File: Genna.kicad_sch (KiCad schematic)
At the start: 12 parts, among them J1 USB_A, J2 Conn_01x09, J3 Conn_01x09, U1 ATmega32U4-M

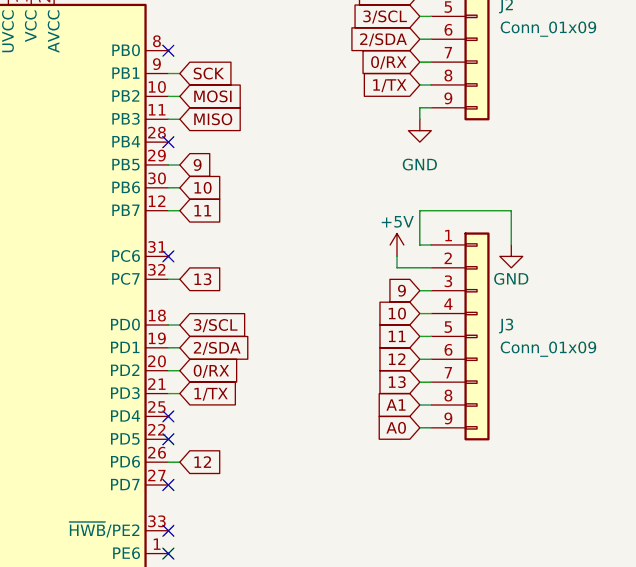
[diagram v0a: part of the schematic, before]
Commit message: changed via dimensions and had to remove an IO
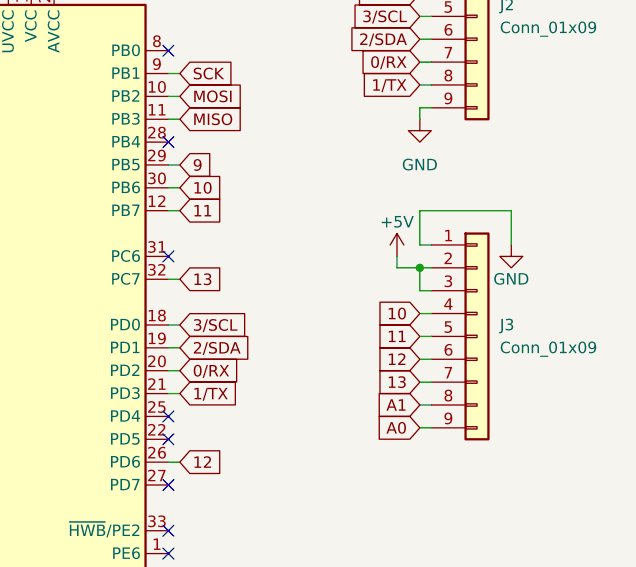
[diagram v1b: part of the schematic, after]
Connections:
- net +5V: now also J3.3 (Pin_3)
- net 9: no longer J3.3 (Pin_3)
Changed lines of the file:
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@@
   (junction (at 168.91 134.62) (diameter 0) (color 0 0 0 0)
+  )
+  (junction (at 214.63 72.39) (diameter 0) (color 0 0 0 0)
   )
   (junction (at 138.43 134.62) (diameter 0) (color 0 0 0 0)
@@
     (stroke (width 0) (type default) (color 0 0 0 0))
   )
+  (wire (pts (xy 214.63 72.39) (xy 215.9 72.39))
+    (stroke (width 0) (type default) (color 0 0 0 0))
+  )
   (wire (pts (xy 154.94 33.02) (xy 171.45 33.02))
     (stroke (width 0) (type default) (color 0 0 0 0))
@@
     (stroke (width 0) (type default) (color 0 0 0 0))
   )
-  (wire (pts (xy 212.09 72.39) (xy 215.9 72.39))
+  (wire (pts (xy 212.09 72.39) (xy 214.63 72.39))
     (stroke (width 0) (type default) (color 0 0 0 0))
   )
@@
     (stroke (width 0) (type default) (color 0 0 0 0))
   )
+  (wire (pts (xy 214.63 72.39) (xy 214.63 74.93))
+    (stroke (width 0) (type default) (color 0 0 0 0))
+  )
   (wire (pts (xy 152.4 33.02) (xy 154.94 33.02))
     (stroke (width 0) (type default) (color 0 0 0 0))
@@
       (effects (font (size 1.27 1.27)) (justify right) hide)
     )
-  )
-  (global_label "9" (shape input) (at 214.63 74.93 180) (fields_autoplaced)
-    (effects (font (size 1.27 1.27)) (justify right))
-    (property "Intersheet References" "${INTERSHEET_REFS}" (id 0) (at 211.0074 74.8506 0)
-      (effects (font (size 1.27 1.27)) (justify right) hide)
-    )
